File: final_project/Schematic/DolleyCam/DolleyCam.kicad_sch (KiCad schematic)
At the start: 14 parts, among them Q1 PN2222A, Q2 PN2222A

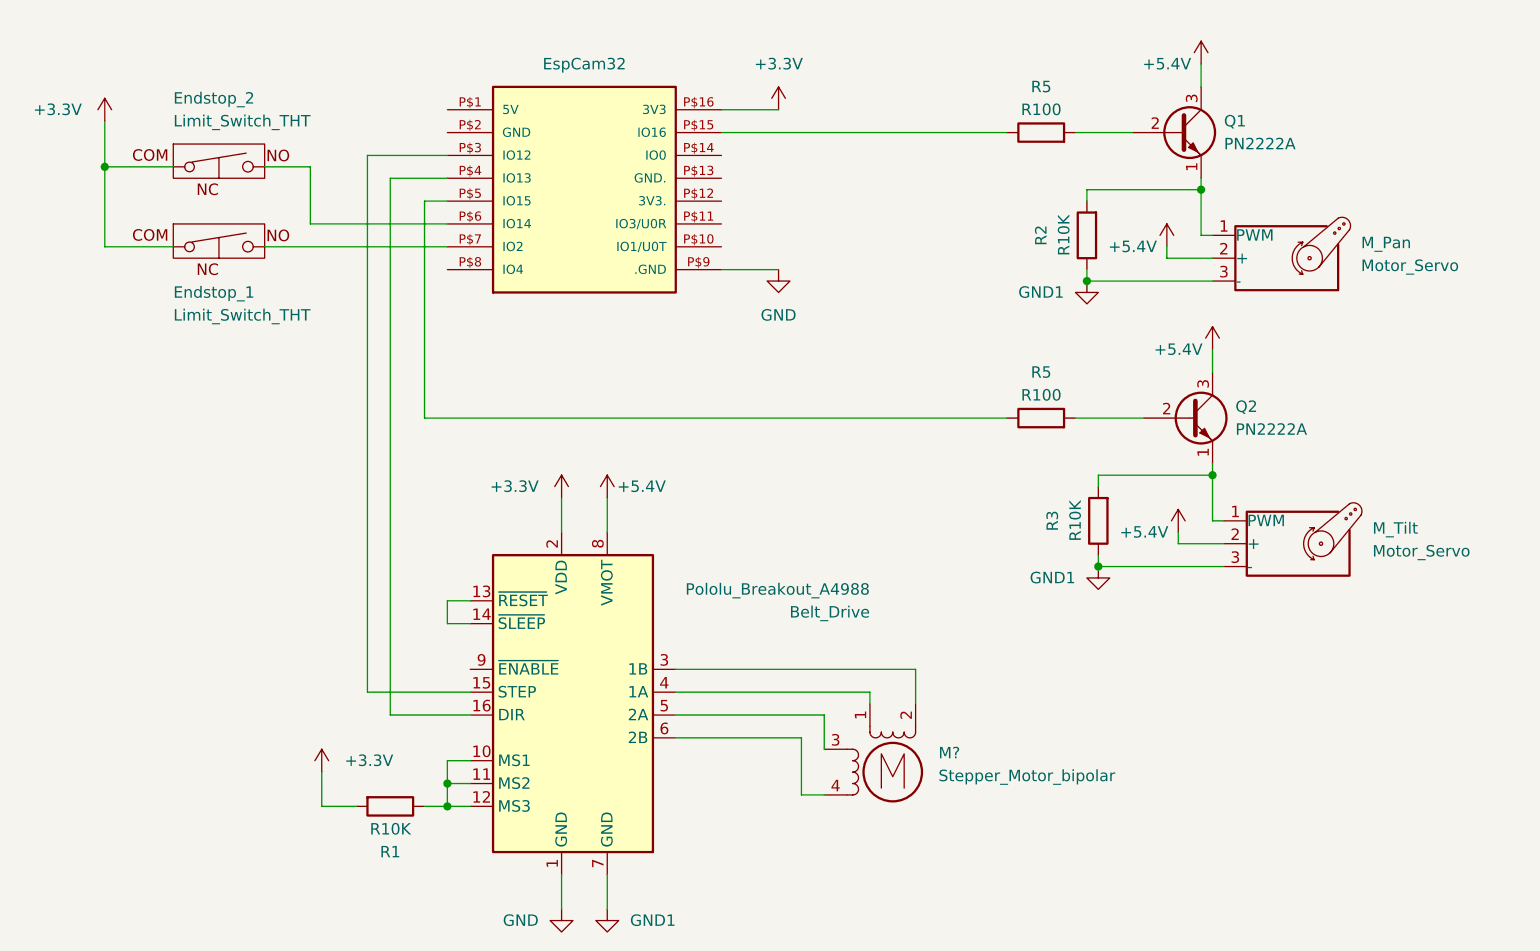
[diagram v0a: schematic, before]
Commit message: update schematic to include capacitors and voltage regulator
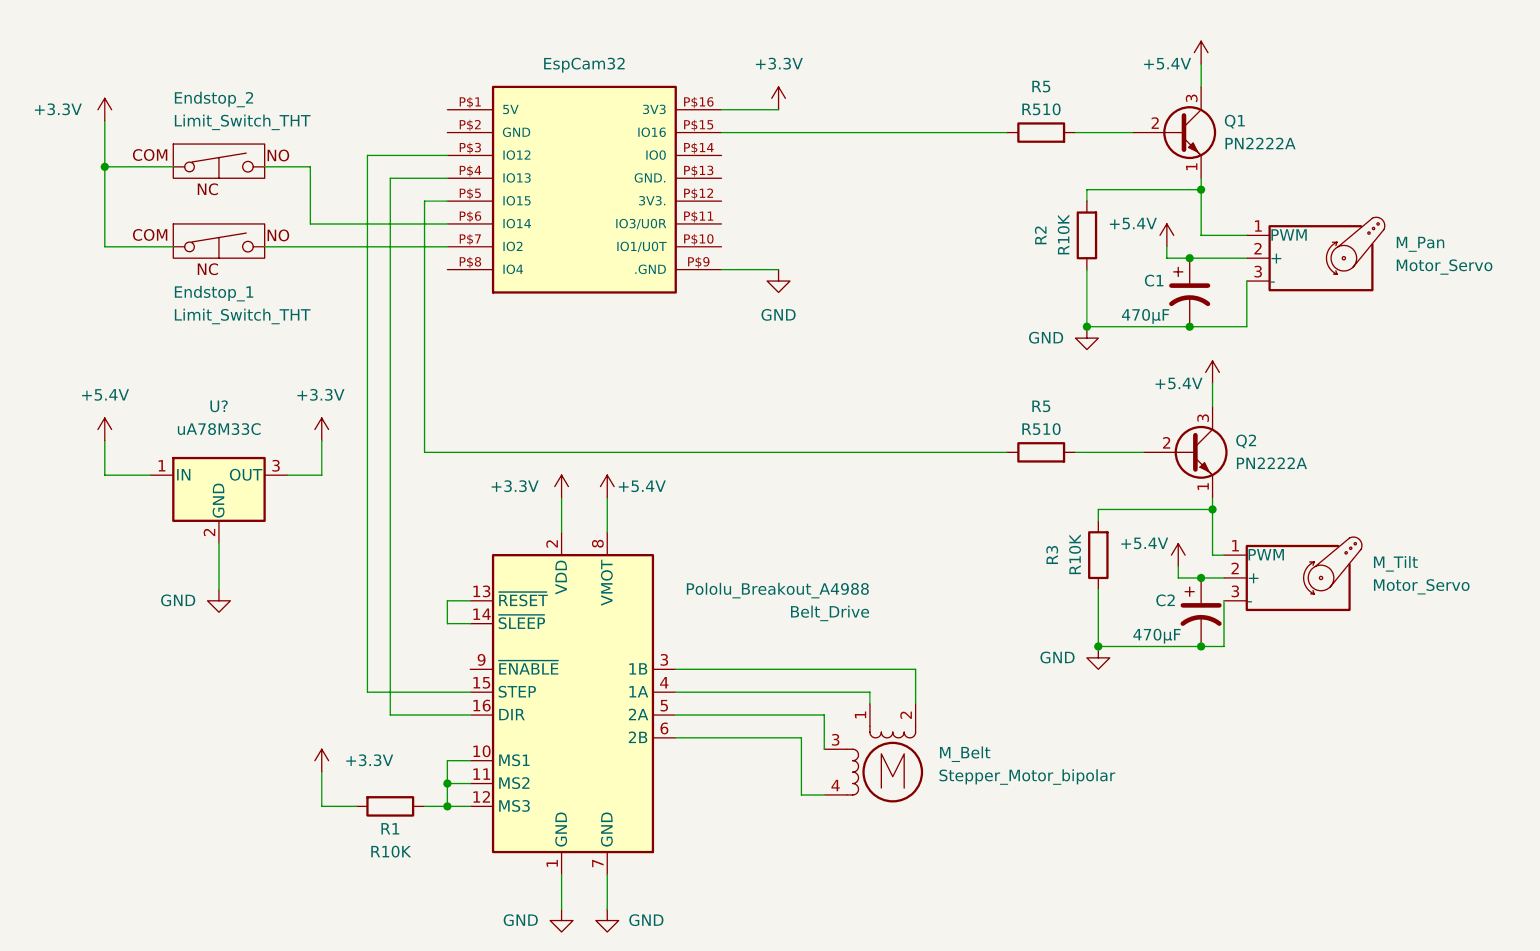
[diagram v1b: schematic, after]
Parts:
- added C1, C2: 470µF, symbol Device:C_Polarized_US
- added U?: uA78M33C, symbol AAAACustom:uA78M33C
- R5: value R100 -> R510
- gave numbers to parts that had none: 1
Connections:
- net GND1 is gone; now on net GND: Belt_Drive.7 (GND), M_Pan.3 (-), M_Tilt.3 (-), R2.1, R3.1
- net +3.3V: now also U?.3 (OUT)
- net +5.4V: now also C1.1, C2.1, U?.1 (IN)
- net GND: now also C1.2, C2.2, U?.2 (GND)
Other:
- moved on the sheet: M_Pan, M_Tilt, Q2, R3, R5

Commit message: update Schematic
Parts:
- removed Q1, Q2: PN2222A, Package_TO_SOT_THT:TO-92_Inline, symbol Transistor_BJT:PN2222A
- removed R2, R3: R10K, symbol Device:R
- removed U?: uA78M33C, symbol AAAACustom:uA78M33C
- added U1: LM7805, Package_TO_SOT_THT:TO-220-3_Vertical, symbol Regulator_Linear:LM7805_TO220
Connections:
- net +3.3V: now also EspCam32.P$12 (3V3.); no longer EspCam32.P$16 (3V3)
- net +5.4V: no longer Belt_Drive.8 (VMOT)
- net GND: now also U1.2 (GND)
- net +5V: now reaches EspCam32.P$1 (5V)
- net +5V: now also U1.3 (VO)
- net at M_Tilt.1 (PWM): now also R5.2
- net at M_Pan.1 (PWM): now also R5.2
- new net +12V: Belt_Drive.8 (VMOT), U1.1 (VI)
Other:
- moved on the sheet: C1, C2, M_Pan, M_Tilt, R5
